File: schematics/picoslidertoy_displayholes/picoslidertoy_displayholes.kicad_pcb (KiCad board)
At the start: 2 copper layers, 165.1 x 76.2 mm, 46 parts, among them SW1 Capacitive Button, SW2 Capacitive Button, SW3 Capacitive Button, SW4 Capacitive Button, SW5 Capacitive Button, SW6 Capacitive Button, SW7 Capacitive Button, SW8 Capacitive Button, SW9 Capacitive Button, U1 Pico

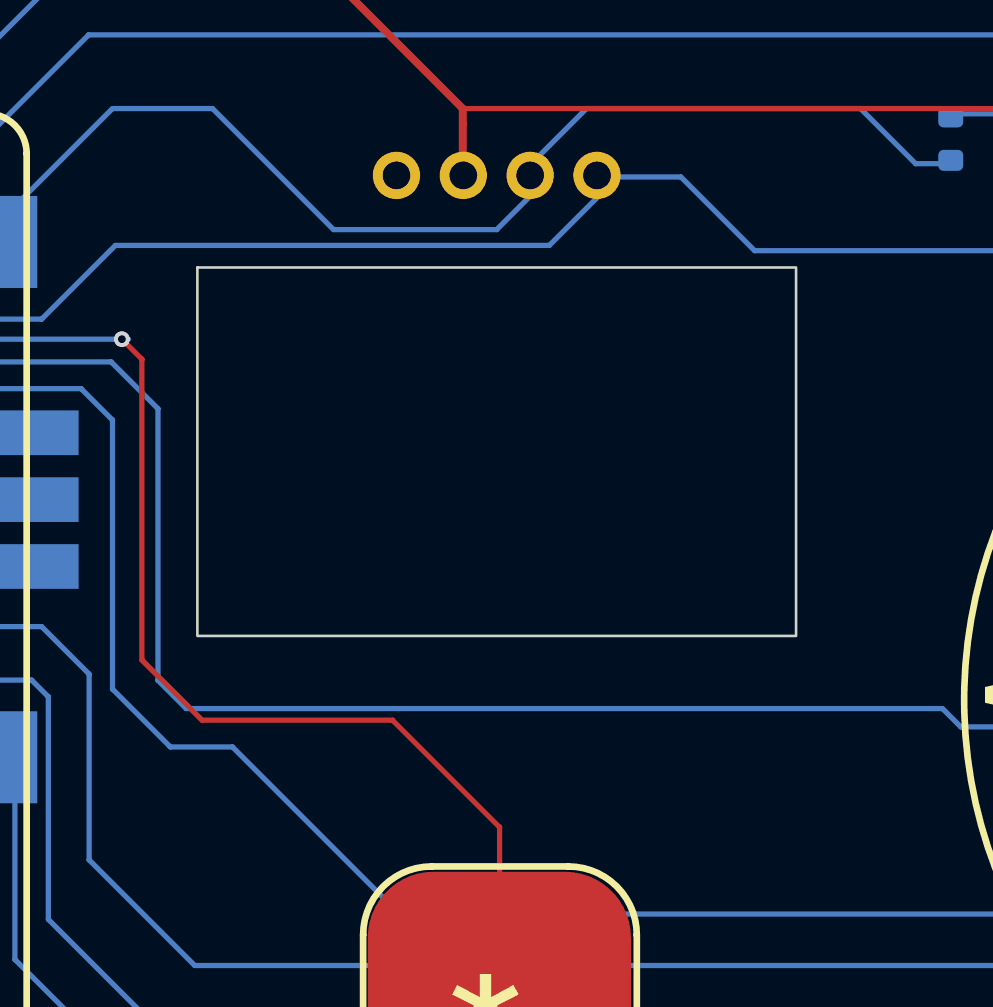
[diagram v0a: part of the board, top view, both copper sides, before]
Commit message: update readme with apps info, new display hole-less version
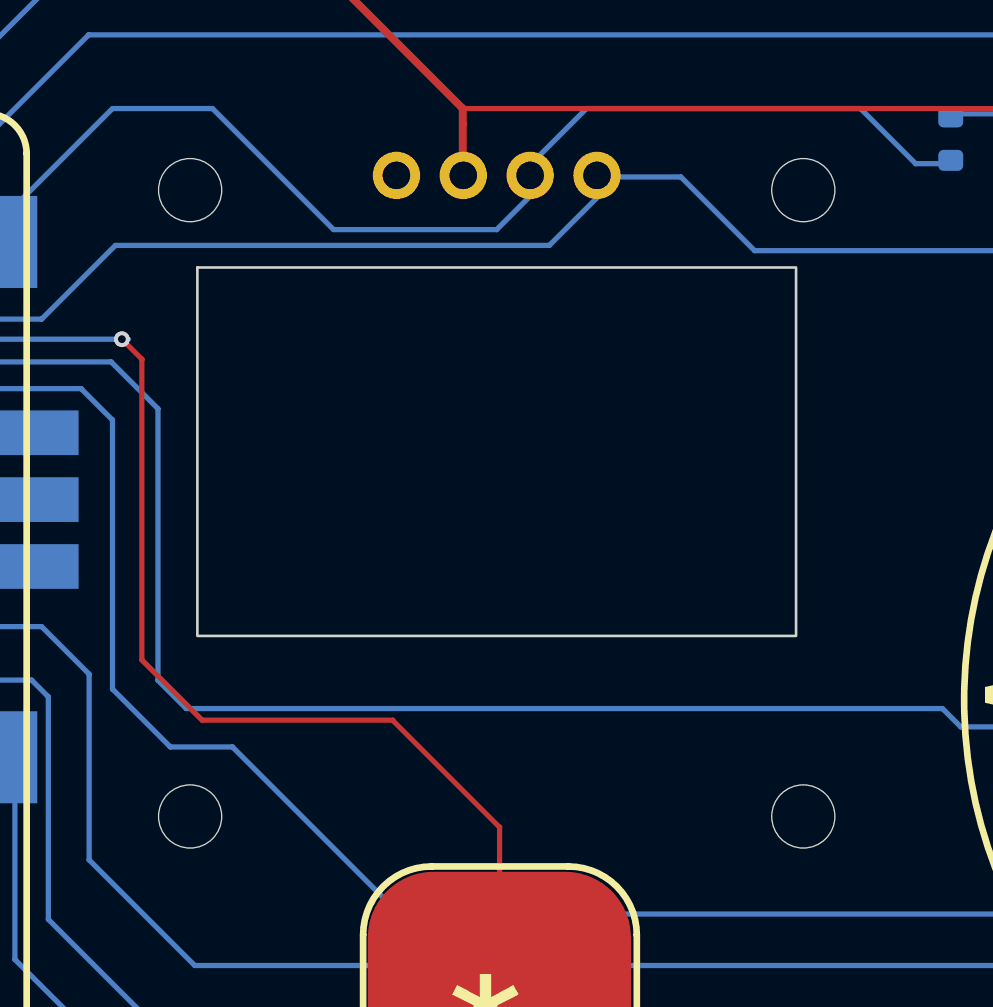
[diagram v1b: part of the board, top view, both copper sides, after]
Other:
- board text added: "picoslidertoy github.com/todbot/picoslidertoy U1: Raspberry Pi Pico DISP1: 1.09{dblquote} I2C OLED SSD1306 R1-R23: 1M R25,R26: 10k 28 Mar 2024"
- board text removed: "picoslidertoy github.com/todbot/picoslidertoy U1: Raspberry Pi Pico DISP1: 0.96{dblquote} I2C OLED SSD1306 R1-R24: 1M R25,R26: 10k 24 Apr 2024 - (no display mounting holes)"
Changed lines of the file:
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@@
 		)
 		(fp_circle
+			(center -11.65 0.56)
+			(end -10.45 0.56)
+			(stroke
+				(width 0.05)
+				(type default)
+			)
+			(fill none)
+			(layer "Edge.Cuts")
+		)
+		(fp_circle
+			(center -11.65 24.36)
+			(end -10.45 24.36)
+			(stroke
+				(width 0.05)
+				(type default)
+			)
+			(fill none)
+			(layer "Edge.Cuts")
+		)
+		(fp_circle
+			(center 11.65 0.56)
+			(end 12.85 0.56)
+			(stroke
+				(width 0.05)
+				(type default)
+			)
+			(fill none)
+			(layer "Edge.Cuts")
+		)
+		(fp_circle
+			(center 11.65 24.36)
+			(end 12.85 24.36)
+			(stroke
+				(width 0.05)
+				(type default)
+			)
+			(fill none)
+			(layer "Edge.Cuts")
+		)
+		(fp_circle
 			(center -13.6 25.6)
 			(end -13.57 25.6)
@@
 		)
 	)
-	(gr_text "picoslidertoy\ngithub.com/todbot/picoslidertoy\nU1: Raspberry Pi Pico\nDISP1: 0.96{dblquote} I2C OLED SSD1306\nR1-R24: 1M\nR25,R26: 10k\n24 Apr 2024 - (no display mounting holes)"
+	(gr_text "picoslidertoy\ngithub.com/todbot/picoslidertoy\nU1: Raspberry Pi Pico\nDISP1: 1.09{dblquote} I2C OLED SSD1306\nR1-R23: 1M\nR25,R26: 10k\n28 Mar 2024"
 		(at 154.432 71.882 0)
 		(layer "B.SilkS")
